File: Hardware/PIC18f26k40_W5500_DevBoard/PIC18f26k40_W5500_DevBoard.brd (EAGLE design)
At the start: 100 x 80 mm, 39 parts, among them J2 MAGJACK, U1 W5500, U2 PIC18F2523-I/SO

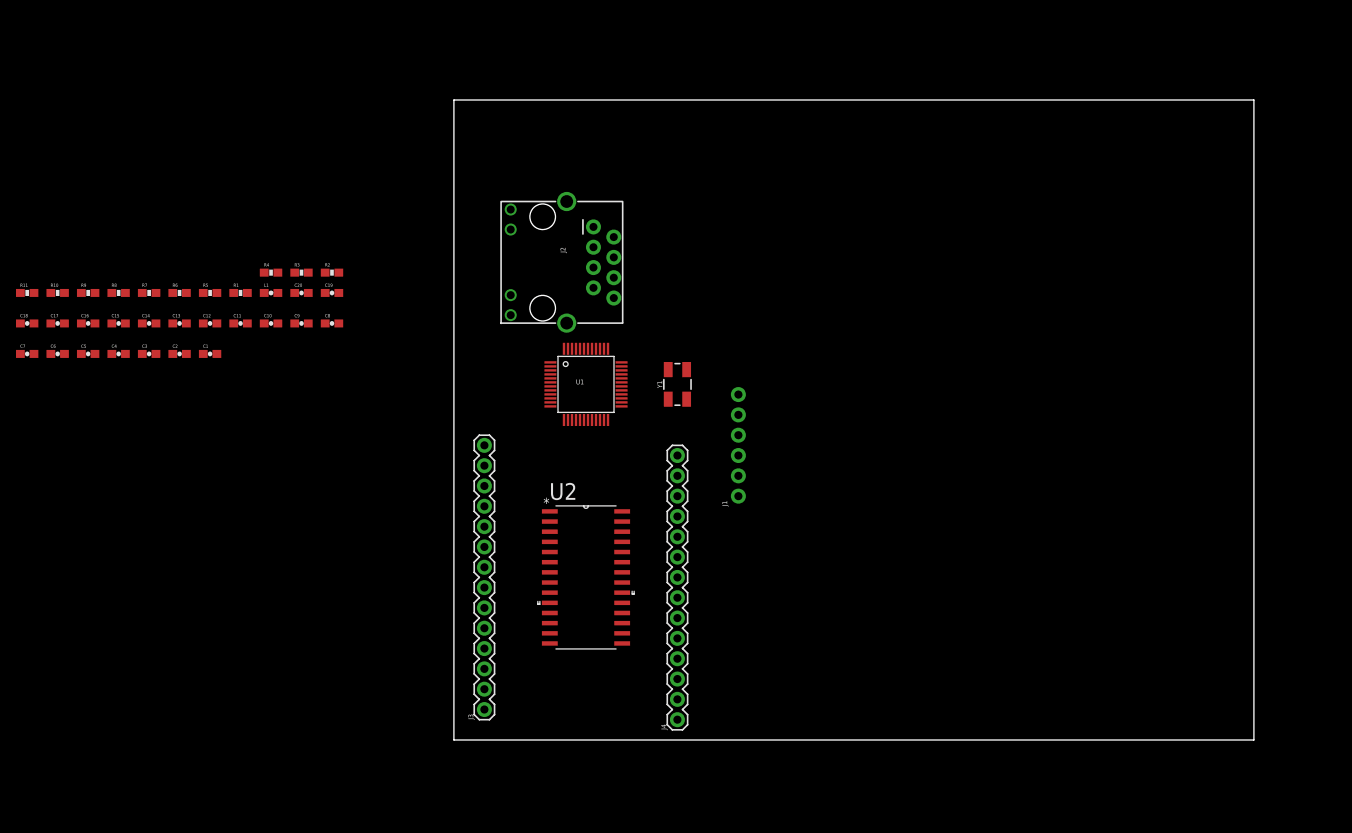
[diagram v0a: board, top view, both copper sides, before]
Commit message: #251 Arranged components on board
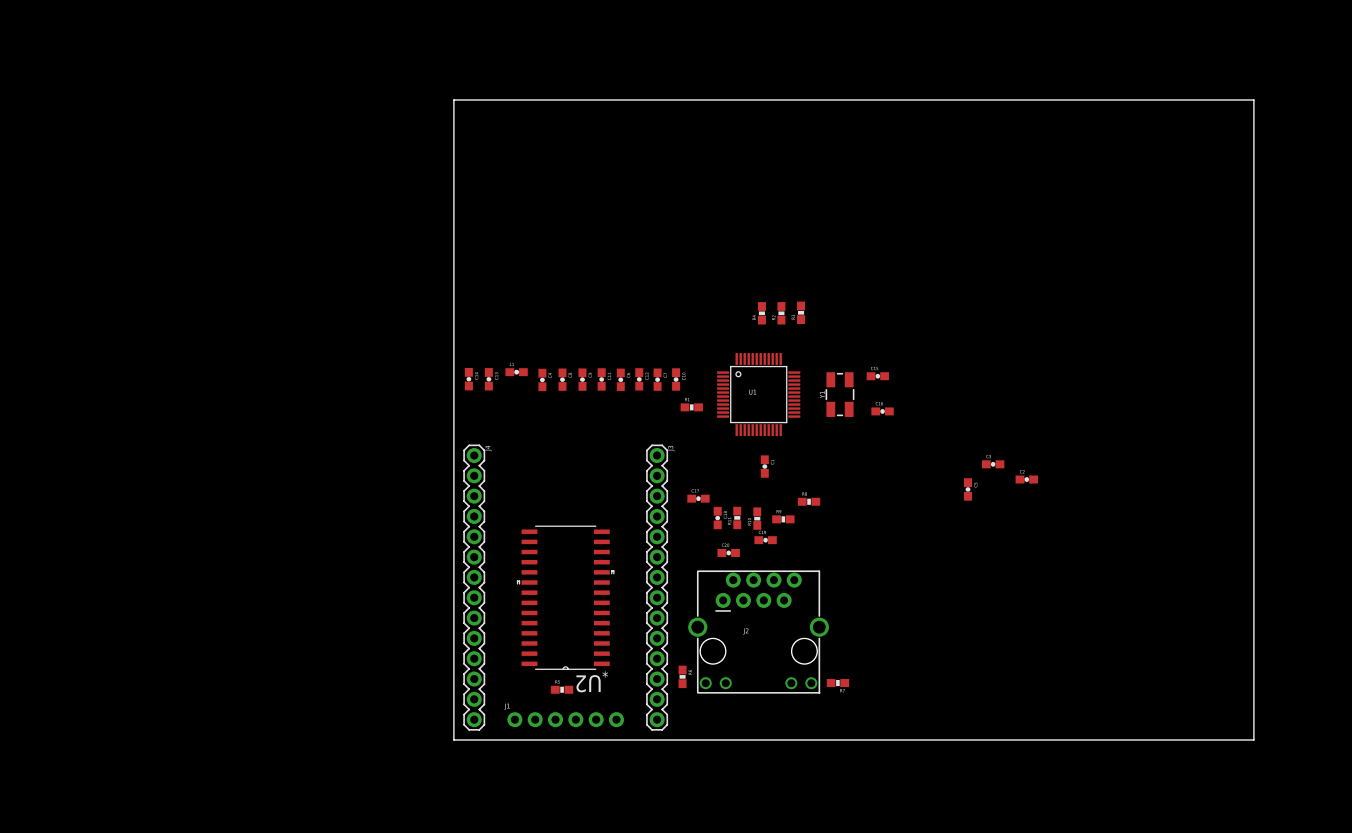
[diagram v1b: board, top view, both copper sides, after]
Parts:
- R2, R3, R4: value (none) -> 10k
- moved C5 111.3 mm to (64.3, 31.3), turned to 270 degrees
- moved C2 107.1 mm to (71.6, 32.6)
- moved C3 106.4 mm to (67.4, 34.5)
- moved C16 99.9 mm to (53.6, 41.1)
- moved R7 98.9 mm to (48.0, 7.12), turned to 180 degrees
- moved C15 95.1 mm to (53.0, 45.5)
- moved R11 93.1 mm to (35.4, 27.8), turned to 90 degrees
- moved R10 91.9 mm to (37.9, 27.7), turned to 90 degrees
- moved R9 91.4 mm to (41.2, 27.6)
- moved R8 90.2 mm to (44.4, 29.8)
- moved C18 89.7 mm to (33.0, 27.7), turned to 270 degrees
- moved C17 83.0 mm to (30.6, 30.2)
- moved R6 79.1 mm to (28.6, 7.89), turned to 270 degrees
- moved C7 78.9 mm to (25.5, 45.0), turned to 270 degrees
- moved J2 73.9 mm to (30.5, 0.00), turned to 0 degrees
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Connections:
- removed net N$3: C10.2, C11.2, C12.2, C13.2, C14.2, C4.2, C6.2, C7.2, C8.2, C9.2
- net GND: now also C10.2, C11.2, C12.2, C13.2, C14.2, C4.2, C6.2, C7.2, C8.2, C9.2

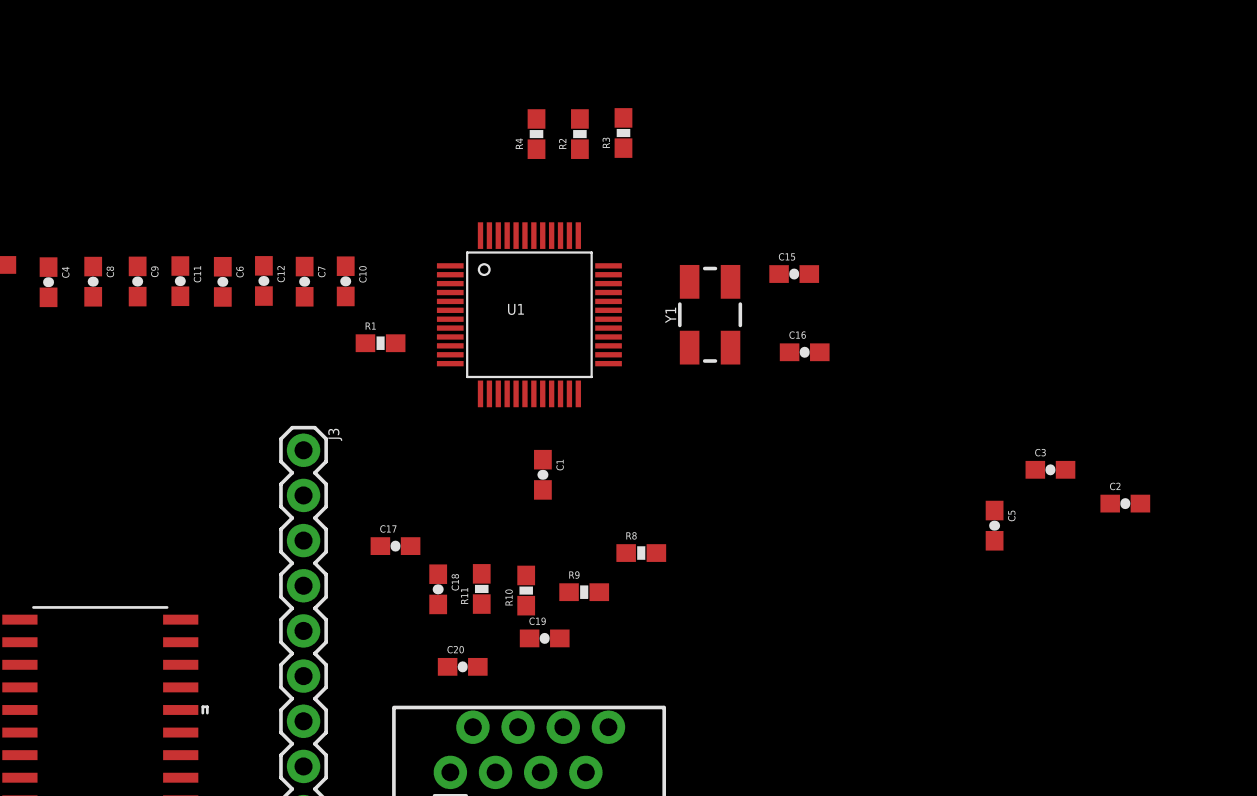
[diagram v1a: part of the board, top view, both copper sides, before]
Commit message: #241 Rearranged parts on board
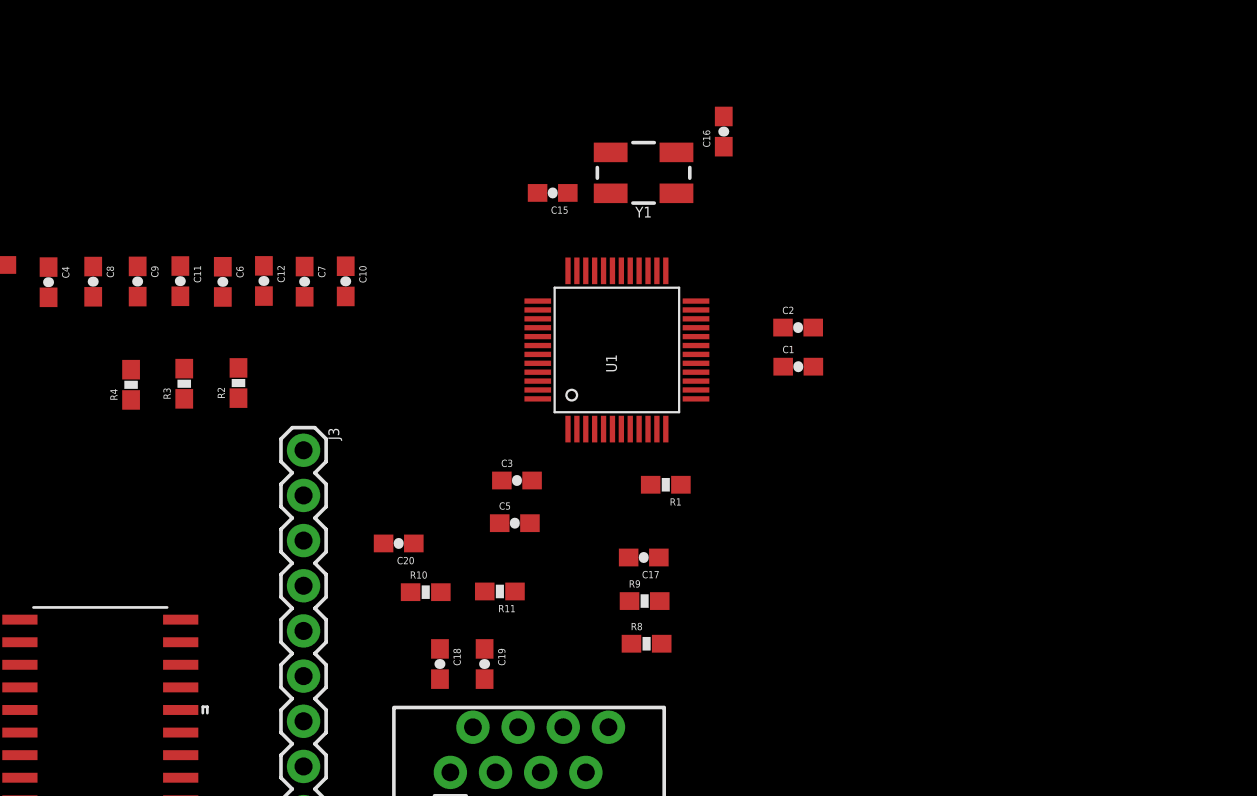
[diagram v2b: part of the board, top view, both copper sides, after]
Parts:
- moved C3 30.0 mm to (37.4, 33.9)
- moved R3 28.4 mm to (18.7, 39.3)
- moved C5 27.0 mm to (37.3, 31.5), turned to 0 degrees
- moved R4 26.8 mm to (15.7, 39.2)
- moved R2 23.8 mm to (21.7, 39.3)
- moved C2 20.9 mm to (53.2, 42.5)
- moved R1 17.9 mm to (45.8, 33.6), turned to 180 degrees
- moved C1 15.6 mm to (53.2, 40.3), turned to 0 degrees
- moved C15 14.3 mm to (39.4, 50.0), turned to 180 degrees
- moved C17 14.0 mm to (44.5, 29.5), turned to 180 degrees
- moved C16 13.2 mm to (49.0, 53.5), turned to 90 degrees
- moved Y1 8.81 mm to (44.5, 51.2), turned to 180 degrees
- moved C20 7.82 mm to (30.8, 30.3), turned to 180 degrees
- moved R10 5.65 mm to (32.3, 27.6), turned to 0 degrees
- moved U1 5.30 mm to (43.0, 41.2), turned to 90 degrees
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
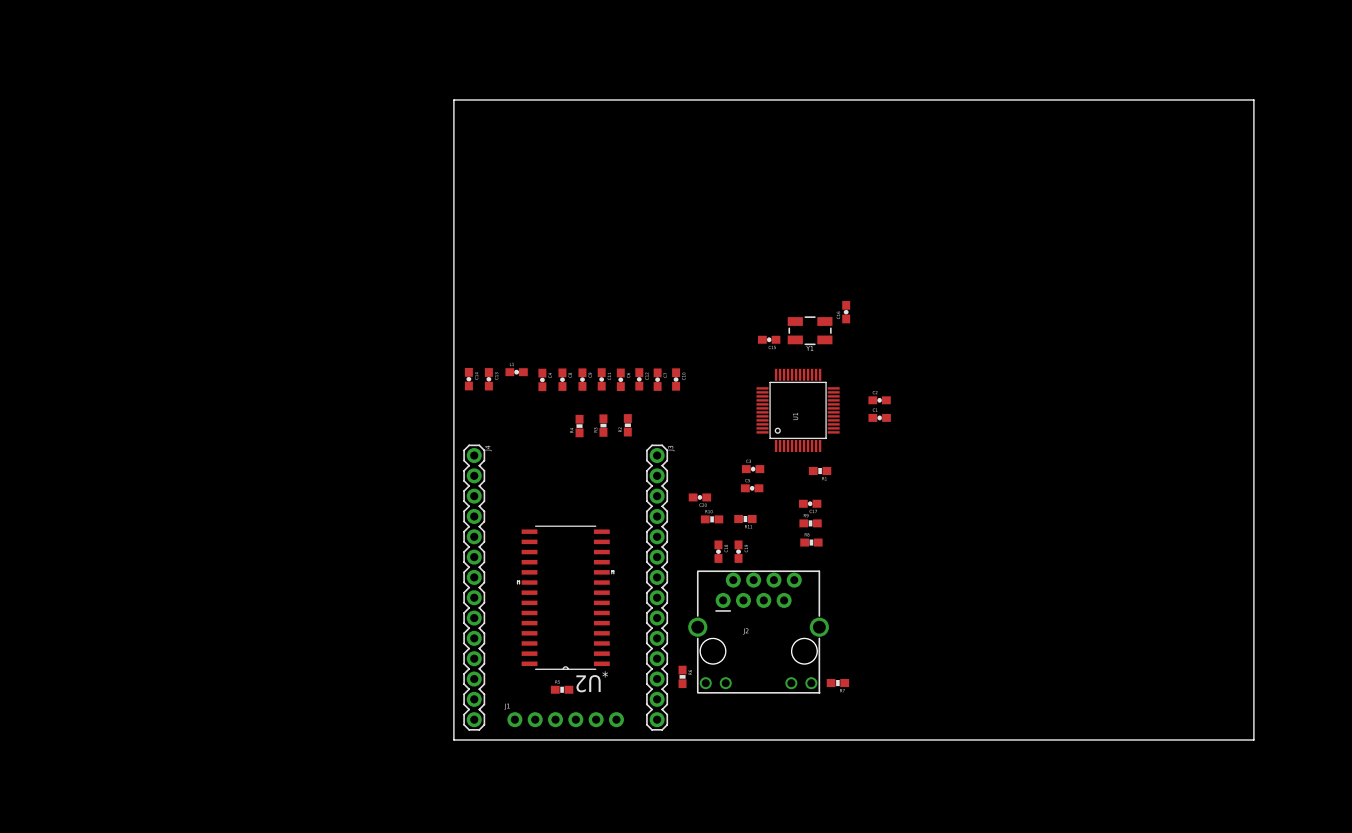
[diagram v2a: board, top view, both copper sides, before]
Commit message: #251 Routed several signals
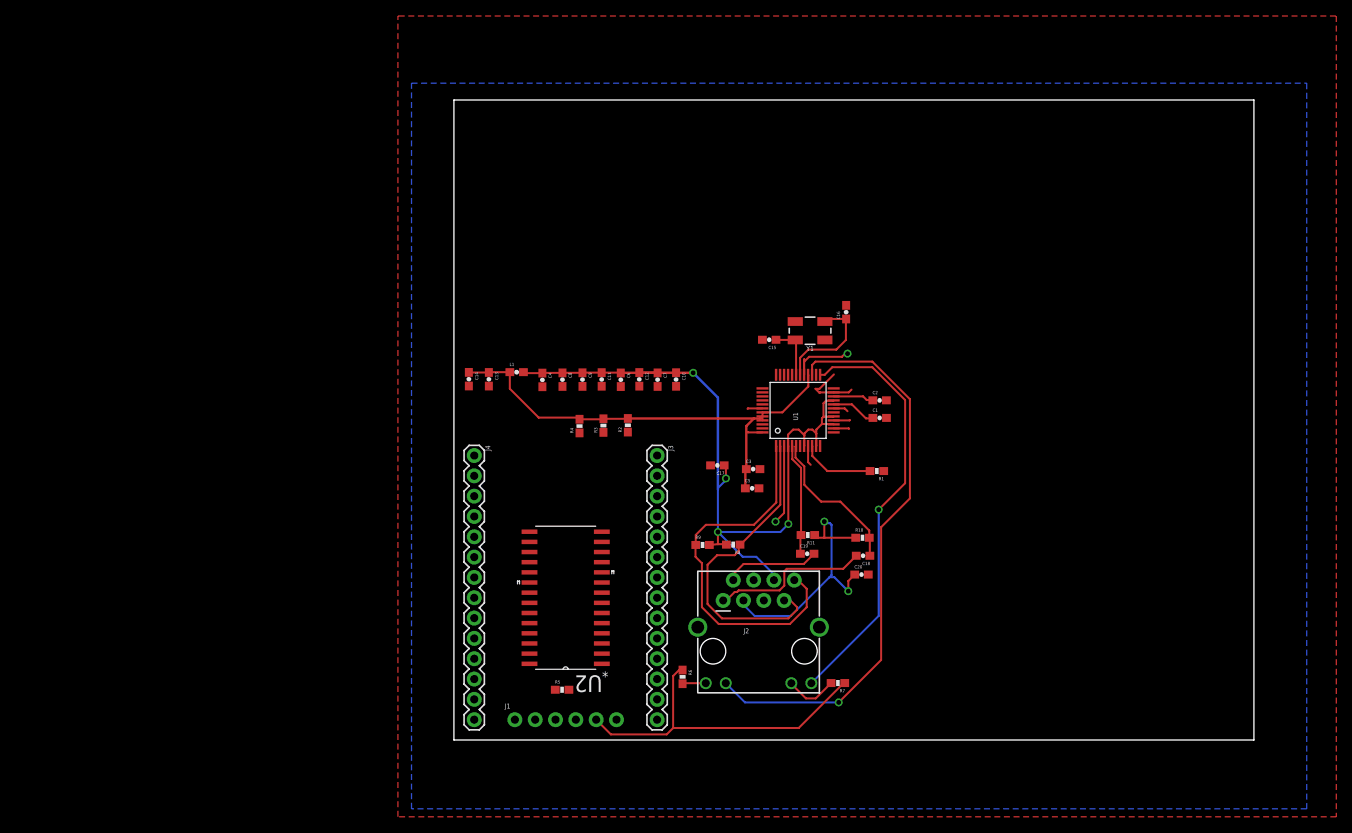
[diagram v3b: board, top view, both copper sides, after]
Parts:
- moved C20 22.4 mm to (51.0, 20.7), turned to 0 degrees
- moved R10 18.9 mm to (51.1, 25.3)
- moved C18 18.1 mm to (51.1, 23.0), turned to 180 degrees
- moved R9 13.8 mm to (31.1, 24.4)
- moved C17 12.6 mm to (32.9, 34.3)
- moved R8 9.78 mm to (34.9, 24.4), turned to 180 degrees
- moved C19 8.58 mm to (44.2, 23.3), turned to 0 degrees
- moved R11 8.05 mm to (44.2, 25.6)
- moved R1 7.10 mm to (52.9, 33.6)
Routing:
- net VCCA: track 0.00 -> 102.9 mm, vias 0 -> 4
- net VCC: track 0.00 -> 101.7 mm
- net ACTLED: track 0.00 -> 72.3 mm, vias 0 -> 1
- net LNKLED: track 0.00 -> 53.0 mm, vias 0 -> 1
- net TDN: track 0.00 -> 47.5 mm
- net GND: track 0.00 -> 39.9 mm, vias 0 -> 2
- net TDP: track 0.00 -> 39.5 mm
- net N$11: track 0.00 -> 34.4 mm, vias 0 -> 2
- net N$8: track 0.00 -> 20.0 mm
- net RDP: track 0.00 -> 19.0 mm
- net N$6: track 0.00 -> 14.2 mm
- net RDN: track 0.00 -> 14.0 mm
- net N$10: track 0.00 -> 11.9 mm
- net N$4: track 0.00 -> 9.26 mm
- net N$5: track 0.00 -> 6.82 mm
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- added copper zone on layer 1, net GND
- added copper zone on layer 16, net GND

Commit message: #251 Board downsized and routedd
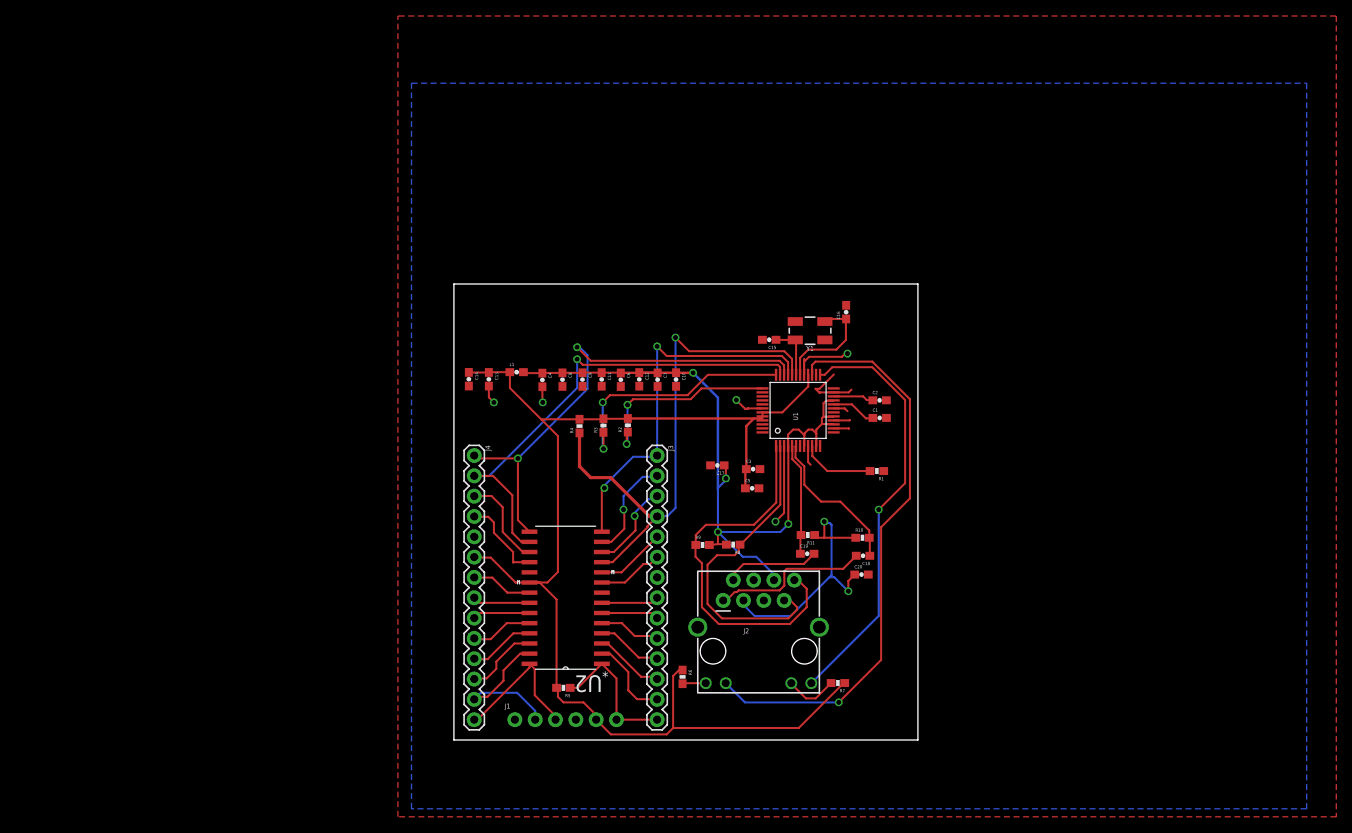
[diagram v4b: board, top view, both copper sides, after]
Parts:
- moved R5 0.29 mm to (13.7, 6.52), turned to 180 degrees
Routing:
- net SCSN: track 0.00 -> 67.5 mm, vias 0 -> 1
- net MISO: track 0.00 -> 61.6 mm, vias 0 -> 2
- net MOSI: track 0.00 -> 60.9 mm, vias 0 -> 1
- net VCC: track 101.7 -> 156.7 mm
- net SCK: track 0.00 -> 46.5 mm, vias 0 -> 2
- net INT: track 0.00 -> 31.0 mm, vias 0 -> 2
- net RST: track 0.00 -> 24.2 mm, vias 0 -> 2
- net PGC: track 0.00 -> 20.0 mm
- net PGD: track 0.00 -> 19.4 mm
- net MCLR: track 0.00 -> 18.0 mm
- net RC2: track 0.00 -> 12.9 mm, vias 0 -> 1
- net RC6: track 0.00 -> 11.6 mm
- net RC1: track 0.00 -> 11.2 mm, vias 0 -> 1
- net RC7: track 0.00 -> 10.8 mm
- net RA0: track 0.00 -> 10.6 mm
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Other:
- board size 100 x 80 mm -> 58 x 57 mm

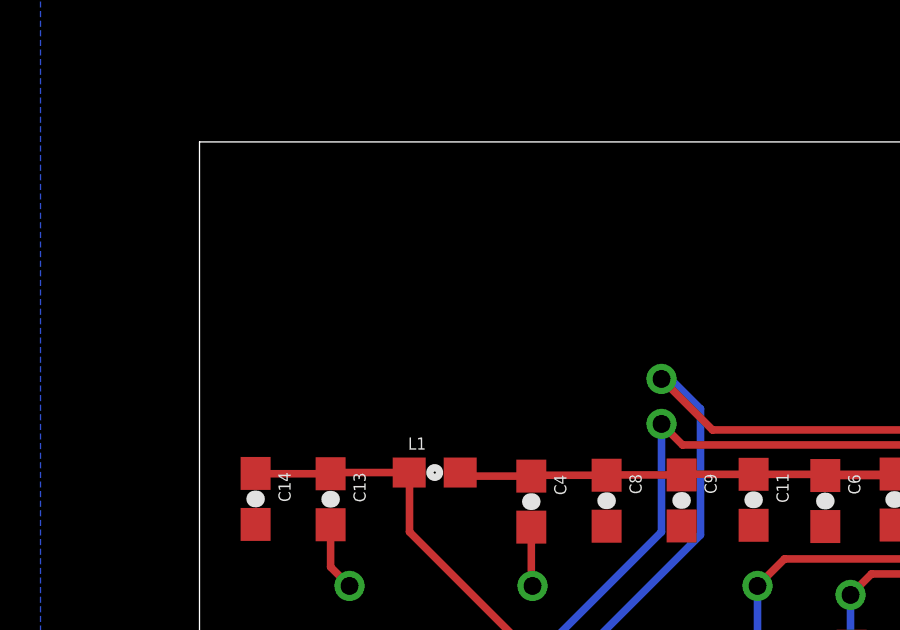
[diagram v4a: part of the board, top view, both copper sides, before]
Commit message: #251 Added logo to W5500 Dev board
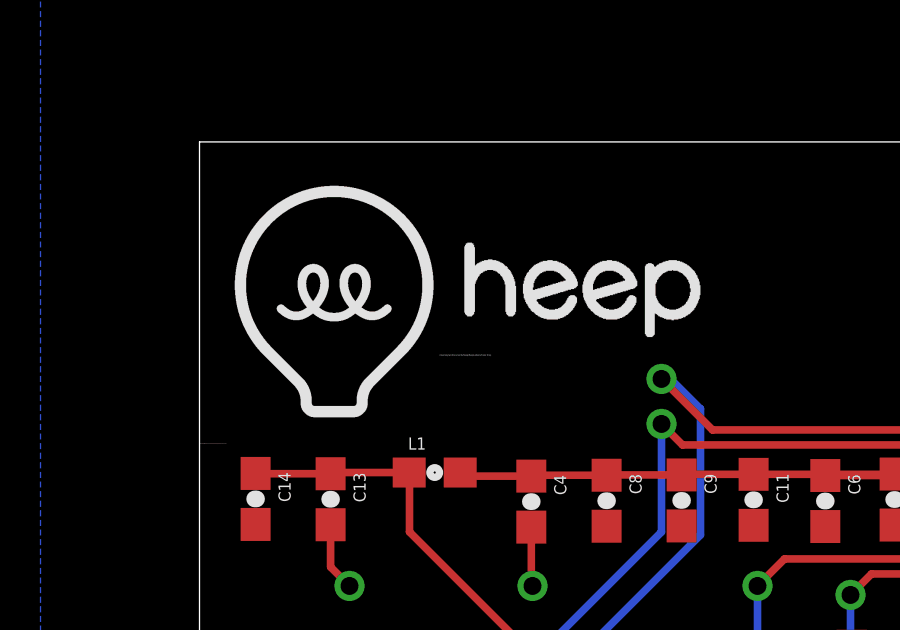
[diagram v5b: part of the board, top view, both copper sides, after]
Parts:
- added U$5: (no value), Heep:HEEPLOGOSMALL
- added U$6: (no value), Heep:HEEPLETTERS
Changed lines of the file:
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@@
 </element>
 <element name="Y1" library="SparkFun-Clocks" package="CRYSTAL-SMD-5X3.2-4PAD" value="" x="44.52" y="51.16" rot="R180"/>
+<element name="U$5" library="Heep" package="HEEPLOGOSMALL" value="" x="0" y="47"/>
+<element name="U$6" library="Heep" package="HEEPLETTERS" value="" x="8" y="50"/>
 </elements>
 <signals>
